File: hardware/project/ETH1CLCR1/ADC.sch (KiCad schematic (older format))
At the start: 53 parts, among them Q1601 BC847, Q1602 BC847, Q1603 BC847, Q1604 BC847, U1601 ADS8363, U1602 INA159, U1603 INA159, U1604 ADG419BR, U1605 ADG419BR, U1606 OPA602, U1607 OPA602, U1608 PGA103, U1609 PGA103

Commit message: Footprint asigment (not finished).
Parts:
- renumbered C1614 to C1501, C1602 to C1502, C1615 to C1503, C1604 to C1504, C1617 to C1505, C1619 to C1506, C1618 to C1507, C1620 to C1508, C1601 to C1509, C1603 to C1510, C1605 to C1511, C1607 to C1512, C1606 to C1513, C1608 to C1514, C1609 to C1515, C1610 to C1516, C1611 to C1517, C1612 to C1518, C1613 to C1519, C1616 to C1520, Q1601 to Q1501, Q1603 to Q1502, Q1602 to Q1503, Q1604 to Q1504, R1601 to R1501, R1615 to R1502, R1607 to R1503, R1609 to R1504, R1611 to R1505, R1603 to R1506, R1612 to R1507, R1604 to R1508, R1605 to R1509, R1606 to R1510, R1602 to R1511, R1616 to R1512, R1608 to R1513, R1610 to R1514, R1613 to R1515, R1614 to R1516, R1617 to R1517, R1619 to R1518, R1618 to R1519, R1620 to R1520, U1602 to U1501, U1604 to U1502, U1608 to U1503, U1606 to U1504, U1601 to U1505, U1603 to U1506, U1605 to U1507, U1609 to U1508, U1607 to U1509
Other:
- moved on the sheet: C1501, C1502, C1503, C1504, R1501, R1502, R1503, R1504, R1505, R1506, R1507, R1508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

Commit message: Redesinged ADC schematic.
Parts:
- removed C1511, C1513, C1515, C1517, C1519: 100n, Capacitor_SMD:C_0603_1608Metric_Pad1.05x0.95mm_HandSolder, symbol Device:C
- removed C1514, C1516, C1518, C1520: 10u, Capacitor_SMD:C_0805_2012Metric_Pad1.15x1.40mm_HandSolder, symbol Device:C
- removed U1501, U1506: INA159, Package_SO:MSOP-8_3x3mm_P0.65mm, symbol ETH1CLCR1:INA159
- removed U1505: ADS8363, Package_DFN_QFN:QFN-32-1EP_5x5mm_P0.5mm_EP3.6x3.6mm_ThermalVias, symbol ETH1CLCR1:ADS8363
- added C1501, C1504, C1505, C1507: 1u, Capacitor_SMD:C_0603_1608Metric_Pad1.05x0.95mm_HandSolder, symbol Device:C
- added C1502, C1506, C1508: 100n, Capacitor_SMD:C_0603_1608Metric_Pad1.05x0.95mm_HandSolder, symbol Device:C
- added R1501, R1502: 100, Resistor_SMD:R_0603_1608Metric_Pad1.05x0.95mm_HandSolder, symbol Device:R
- added R1503, R1504, R1512, R1514: 10k, Resistor_SMD:R_0603_1608Metric_Pad1.05x0.95mm_HandSolder, symbol Device:R
- added R1507, R1515, R1516: 52k3, Resistor_SMD:R_0603_1608Metric_Pad1.05x0.95mm_HandSolder, symbol Device:R
- added R1513: 12k, Resistor_SMD:R_0603_1608Metric_Pad1.05x0.95mm_HandSolder, symbol Device:R
- added U1503: AD8606-2-MSOP, symbol ETH1CLCR1:AD8606-2-MSOP
- added U1504: AD7380, symbol ETH1CLCR1:AD7380
- added U1505: AD8605, symbol ETH1CLCR1:AD8605
- C1503: value 1n -> 100n
- C1510: value 10u -> 100n; footprint Capacitor_SMD:C_0805_2012Metric_Pad1.15x1.40mm_HandSolder -> Capacitor_SMD:C_0603_1608Metric_Pad1.05x0.95mm_HandSolder
- C1512: value 10u -> 1n; footprint Capacitor_SMD:C_0805_2012Metric_Pad1.15x1.40mm_HandSolder -> Capacitor_SMD:C_0603_1608Metric_Pad1.05x0.95mm_HandSolder
- R1506: value 0 -> 100
- R1508: value 0 -> 52k3
- R1509, R1510: value 0 -> 12k
- R1511: value 100 -> 12k
- renumbered C1501 to C1511, C1505 to C1513, C1507 to C1514, C1502 to C1515, C1504 to C1516, C1506 to C1517, C1508 to C1518, Q1503 to Q1502, Q1502 to Q1503, R1501 to R1505, R1503 to R1517, R1513 to R1518, R1504 to R1519, R1514 to R1520, R1505 to R1521, R1507 to R1522, R1515 to R1523, R1516 to R1524, R1517 to R1525, R1519 to R1526, R1502 to R1527, R1512 to R1528, R1518 to R1529, R1520 to R1530, U1507 to U1501, U1504 to U1506, U1509 to U1507, U1503 to U1508, U1508 to U1509
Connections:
- net labels added: ADC_REF, ADC_SCLK, ADC_~ALARM, REFIO
- net labels removed: ADC_BUSY, ADC_CLOCK, ADC_CONVST, ADC_RD
- wire segments 246 -> 207
- no-connect marks 7 -> 4
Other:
- moved on the sheet: C1511, C1515, C1516, R1505, R1517, R1518, R1519, R1520, R1521, R1522, R1523, R1524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

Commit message: Redesigned the power supply, added humidy+temp. sensor.
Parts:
- removed R1503, R1504: 10k, Resistor_SMD:R_0603_1608Metric_Pad1.05x0.95mm_HandSolder, symbol Device:R
- added C1103, C1105: 1u, Capacitor_SMD:C_0603_1608Metric_Pad1.05x0.95mm_HandSolder, symbol Device:C
- added C1108, C1109: 3300p, Capacitor_SMD:C_0603_1608Metric_Pad1.05x0.95mm_HandSolder, symbol Device:C
- added C1110, C1111, C1112, C1113: 100n, Capacitor_SMD:C_0603_1608Metric_Pad1.05x0.95mm_HandSolder, symbol Device:C
- added R1103, R1104: 1k, Resistor_SMD:R_0603_1608Metric_Pad1.05x0.95mm_HandSolder, symbol Device:R
- added R1105, R1106, R1107, R1108: 100, Resistor_SMD:R_0603_1608Metric_Pad1.05x0.95mm_HandSolder, symbol Device:R
- added R1109, R1110, R1111, R1112: 50, Resistor_SMD:R_0603_1608Metric_Pad1.05x0.95mm_HandSolder, symbol Device:R
- added U1105: AD8605, Package_TO_SOT_SMD:SOT-23-5_HandSoldering, symbol ETH1CLCR1:AD8605
- added U1107, U1108: LT6350, Package_SO:MSOP-8_3x3mm_P0.65mm, symbol ETH1CLCR1:LT6350
- U1103: renamed from U1503; footprint (none) -> Package_SO:MSOP-8_3x3mm_P0.65mm
- U1104: renamed from U1504; footprint (none) -> Package_CSP:LFCSP-16-1EP_3x3mm_P0.5mm_EP1.6x1.6mm
- U1106: renamed from U1505; footprint (none) -> Package_TO_SOT_SMD:SOT-23-5_HandSoldering
- renumbered C1501 to C1101, C1503 to C1102, C1507 to C1104, C1504 to C1106, C1505 to C1107, C1502 to C1114, C1511 to C1115, C1512 to C1116, C1506 to C1117, C1508 to C1118, C1509 to C1119, C1510 to C1120, C1513 to C1121, C1514 to C1122, C1515 to C1123, C1516 to C1124, C1517 to C1125, C1518 to C1126, Q1501 to Q1101, Q1502 to Q1102, Q1503 to Q1103, Q1504 to Q1104, R1501 to R1101, R1502 to R1102, R1507 to R1113, R1505 to R1114, R1508 to R1115, R1506 to R1116, R1509 to R1117, R1510 to R1118, R1511 to R1119, R1512 to R1120, R1513 to R1121, R1514 to R1122, R1515 to R1123, R1516 to R1124, R1517 to R1125, R1518 to R1126, R1519 to R1127, R1520 to R1128, R1521 to R1129, R1522 to R1130, R1523 to R1131, R1524 to R1132, R1525 to R1133, R1526 to R1134, R1527 to R1135, R1528 to R1136, R1529 to R1137, R1530 to R1138, U1501 to U1101, U1502 to U1102, U1506 to U1109, U1507 to U1110, U1508 to U1111, U1509 to U1112
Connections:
- net +3.3VF: now also C1103.1, C1105.1
- net +5VF: now also C1110.1, C1111.1, C1112.1, C1113.1, U1105.5 (V+), U1107.3 (V+), U1107.7 (~SHDN), U1108.3 (V+), U1108.7 (~SHDN)
- net ADC_REF: now also U1105.1, U1105.4 (-); no longer U1106.1, U1106.4 (-)
- net AGNDF: now also C1103.2, C1105.2, C1110.2, C1111.2, C1112.2, C1113.2, R1104.2, U1105.2 (V-), U1107.6 (V-), U1108.6 (V-)
- net REFIO: now also R1103.2, U1105.3 (+); no longer U1106.3 (+)
- net at C1115.1, R1114.2: now also U1107.8 (+IN1); no longer U1104.8 (AINA+)
- net at C1116.1, R1116.2: now also U1108.8 (+IN1); no longer U1104.6 (AINB+)
- net at U1104.7 (AINA-): now also R1106.2; no longer U1104.5 (AINB-)
- new net: R1103.1, R1104.1, U1106.3 (+)
- new net: R1109.1, U1107.1 (-IN1), U1107.4 (OUT1)
- new net: R1110.1, U1107.5 (OUT2)
- new net: R1111.1, U1108.1 (-IN1), U1108.4 (OUT1)
- new net: R1112.1, U1108.5 (OUT2)
- new net: C1108.1, R1105.1, R1109.2
- new net: C1108.2, R1106.1, R1110.2
- new net: R1105.2, U1104.8 (AINA+)
- new net: C1109.1, R1107.1, R1111.2
- new net: C1109.2, R1108.1, R1112.2
- new net: R1107.2, U1104.6 (AINB+)
- new net: R1108.2, U1104.5 (AINB-)
- new net VCM: U1106.1, U1106.4 (-), U1107.2 (+IN2), U1108.2 (+IN2)
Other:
- moved on the sheet: C1101, C1102, C1104, C1106, C1107, C1114, C1117, C1118, C1119, C1120, R1101, R1102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

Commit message: PCB layout
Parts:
- added R1139, R1140: 499, Resistor_SMD:R_0603_1608Metric_Pad1.05x0.95mm_HandSolder, symbol Device:R
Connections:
- net VCM: now also R1139.2, R1140.2; no longer U1107.2 (+IN2), U1108.2 (+IN2)
- new net: R1139.1, U1107.2 (+IN2)
- new net: R1140.1, U1108.2 (+IN2)
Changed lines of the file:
@@
 	1    0    0    -1
 $EndComp
-Text Label 7600 3150 1    50   ~ 0
+Text Label 7600 3450 1    50   ~ 0
 VCM
 Wire Wire Line
-	7600 3150 7600 2950
-Text Label 7600 6050 1    50   ~ 0
-VCM
-Wire Wire Line
-	7600 6050 7600 5850
-Wire Wire Line
-	7900 5850 7900 6150
-Wire Wire Line
-	7900 6150 6450 6150
-Wire Wire Line
-	6450 6150 6450 5050
+	7600 3450 7600 3250
 Wire Wire Line
 	6450 5050 6550 5050
 Wire Wire Line
-	7900 2950 7900 3250
-Wire Wire Line
-	7900 3250 6450 3250
-Wire Wire Line
-	6450 3250 6450 2150
+	7900 2950 7900 3550
+Wire Wire Line
+	7900 3550 6450 3550
+Wire Wire Line
+	6450 3550 6450 2150
 Wire Wire Line
 	6550 2150 6450 2150
@@
 	1    0    0    -1
 $EndComp
+$Comp
+L Device:R R1139
+U 1 1 5E246E09
+P 7600 3100
+F 0 "R1139" H 7650 3150 50  0000 L CNN
+F 1 "499" H 7670 3055 50  0000 L CNN
+F 2 "Resistor_SMD:R_0603_1608Metric_Pad1.05x0.95mm_HandSolder" V 7530 3100 50  0001 C CNN
+F 3 "~" H 7600 3100 50  0001 C CNN
+	1    7600 3100
+	1    0    0    -1
+$EndComp
+Wire Wire Line
+	7900 5850 7900 6450
+Wire Wire Line
+	7900 6450 6450 6450
+Wire Wire Line
+	6450 5050 6450 6450
+Text Label 7600 6350 1    50   ~ 0
+VCM
+Wire Wire Line
+	7600 6350 7600 6150
+$Comp
+L Device:R R1140
+U 1 1 5E310DDA
+P 7600 6000
+F 0 "R1140" H 7650 6050 50  0000 L CNN
+F 1 "499" H 7670 5955 50  0000 L CNN
+F 2 "Resistor_SMD:R_0603_1608Metric_Pad1.05x0.95mm_HandSolder" V 7530 6000 50  0001 C CNN
+F 3 "~" H 7600 6000 50  0001 C CNN
+	1    7600 6000
+	1    0    0    -1
+$EndComp

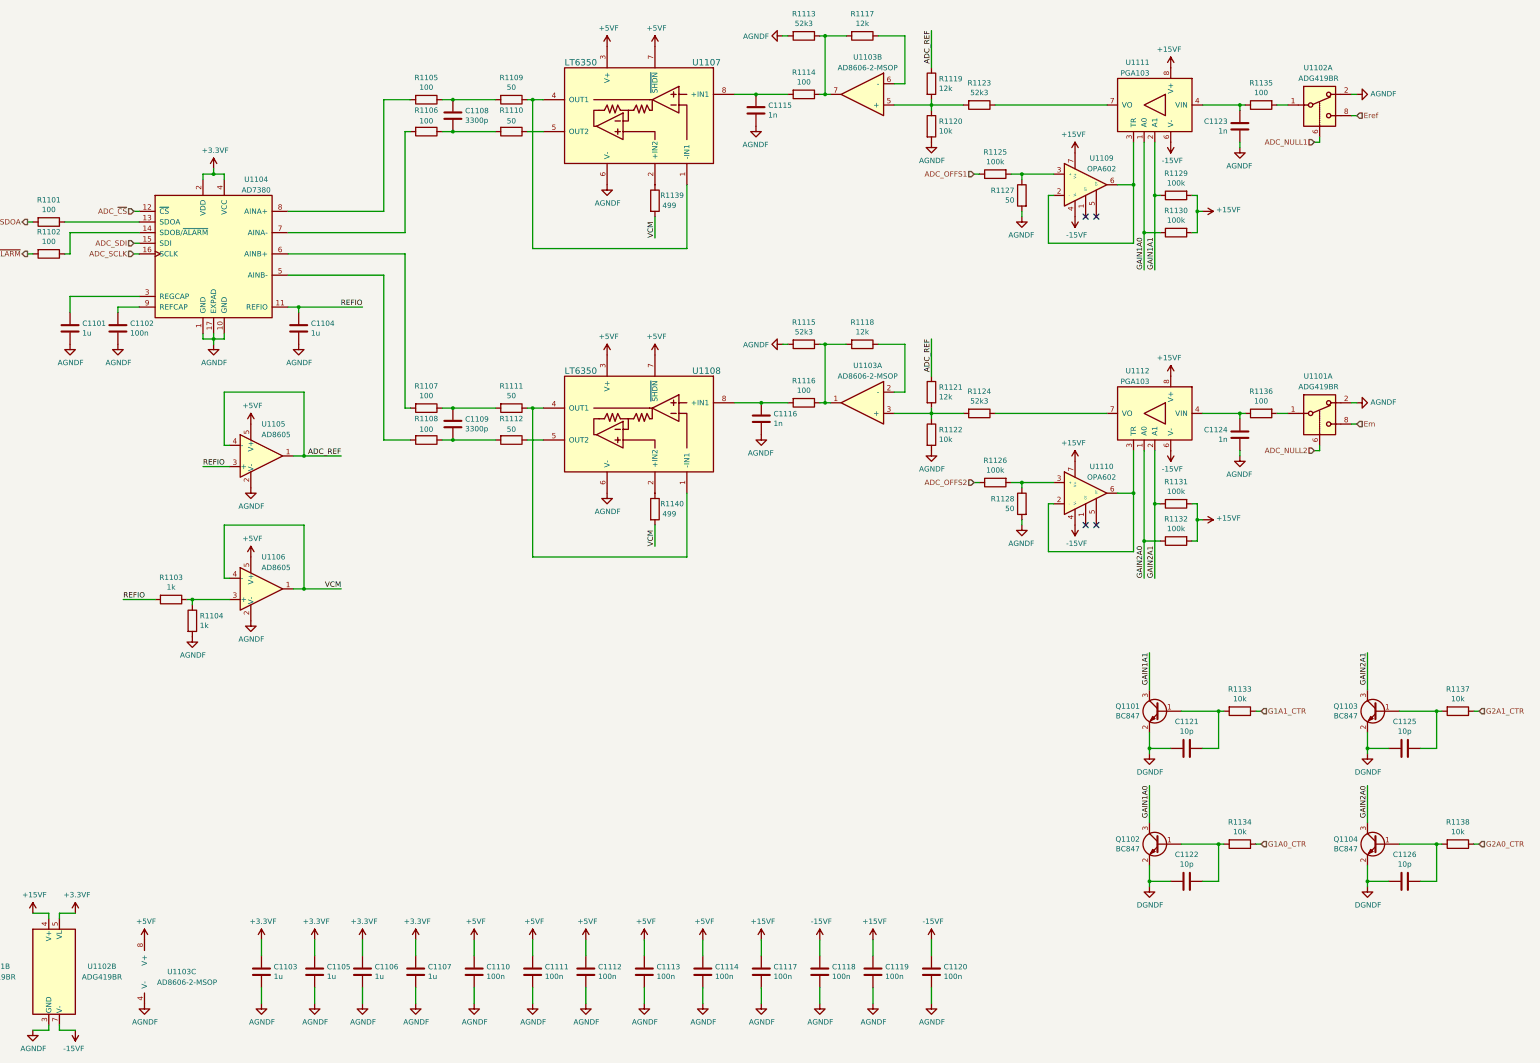
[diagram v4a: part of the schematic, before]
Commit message: Fixed mistake in ADC schematic.
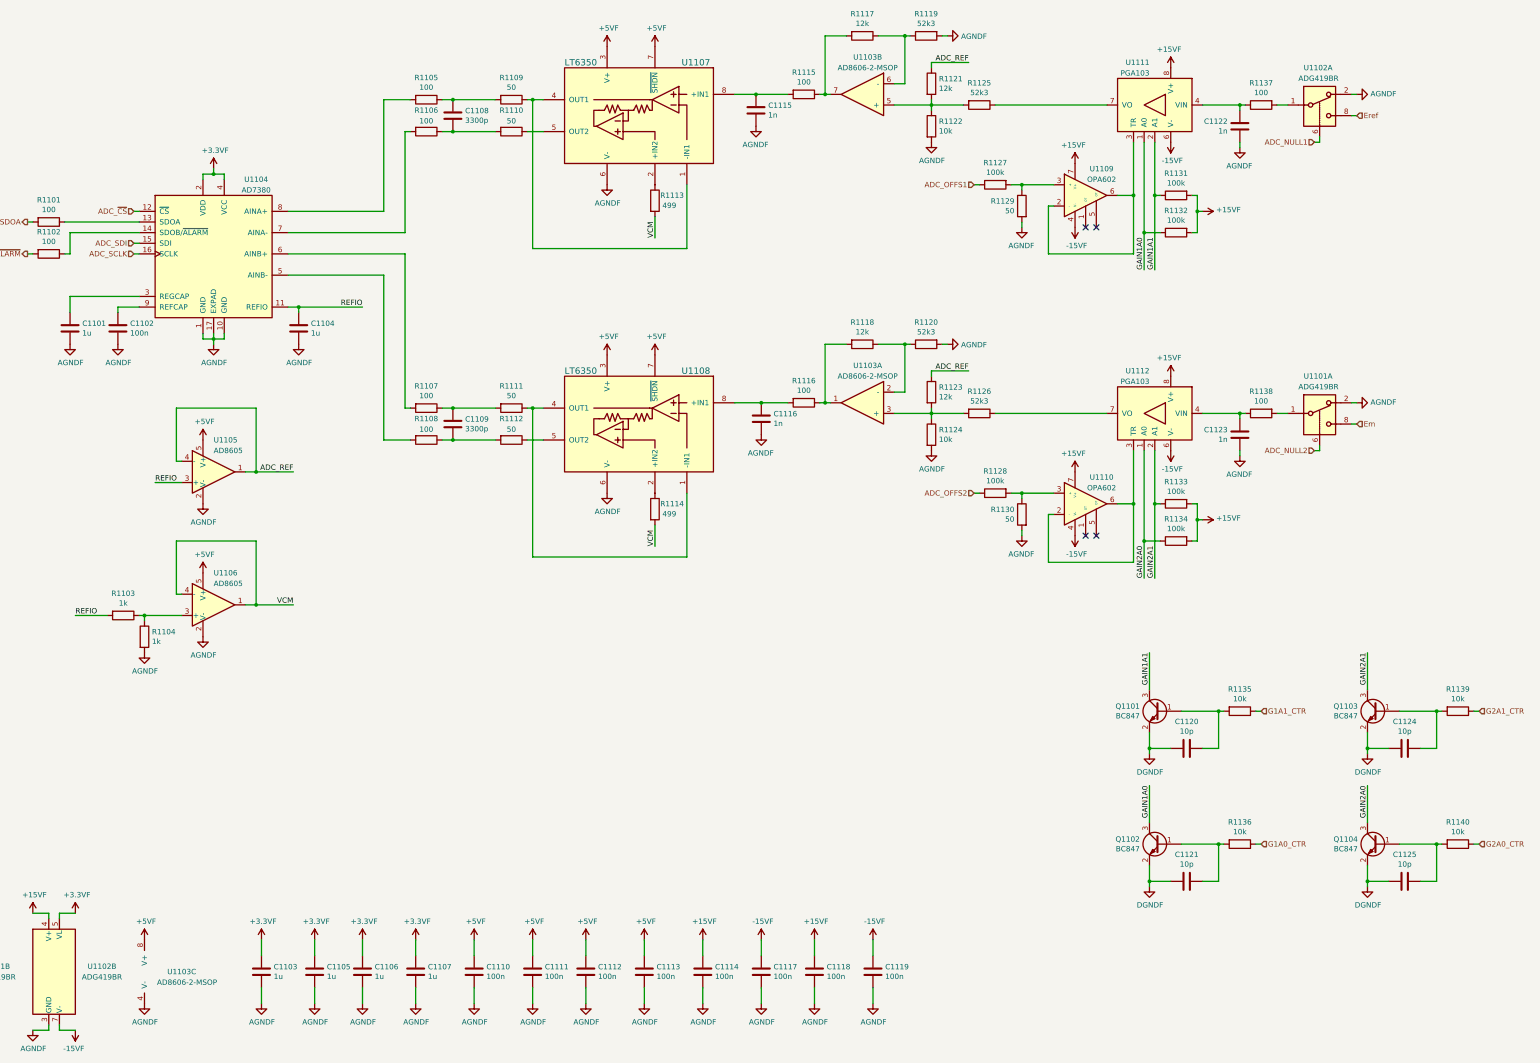
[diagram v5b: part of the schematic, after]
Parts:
- removed C1114: 100n, Capacitor_SMD:C_0603_1608Metric_Pad1.05x0.95mm_HandSolder, symbol Device:C
- renumbered C1117 to C1114, C1118 to C1117, C1119 to C1118, C1120 to C1119, C1121 to C1120, C1122 to C1121, C1123 to C1122, C1124 to C1123, C1125 to C1124, C1126 to C1125, R1139 to R1113, R1140 to R1114, R1114 to R1115, R1113 to R1119, R1115 to R1120, R1119 to R1121, R1120 to R1122, R1121 to R1123, R1122 to R1124, R1123 to R1125, R1124 to R1126, R1125 to R1127, R1126 to R1128, R1127 to R1129, R1128 to R1130, R1129 to R1131, R1130 to R1132, R1131 to R1133, R1132 to R1134, R1133 to R1135, R1134 to R1136, R1135 to R1137, R1136 to R1138, R1137 to R1139, R1138 to R1140
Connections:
- net at R1115.1, R1117.2, U1103.7: no longer R1119.1
- net at R1117.1, U1103.6 (-): now also R1119.1
- net at R1116.1, R1118.2, U1103.1: no longer R1120.1
- net at R1118.1, U1103.2 (-): now also R1120.1
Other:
- moved on the sheet: C1114, C1117, C1118, C1119, R1103, R1104, R1119, R1120, R1127, R1128, R1129, R1130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

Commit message: Changes in schematics.
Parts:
- removed U1105, U1106: AD8605, Package_TO_SOT_SMD:SOT-23-5_HandSoldering, symbol ETH1CLCR1:AD8605
- added C1101, C1106, C1114: 100n, Capacitor_SMD:C_0603_1608Metric_Pad1.05x0.95mm_HandSolder, symbol Device:C
- added C1102: 10u, Capacitor_SMD:C_0805_2012Metric_Pad1.15x1.40mm_HandSolder, symbol Device:C
- added C1104: 1u, Capacitor_SMD:C_0603_1608Metric_Pad1.05x0.95mm_HandSolder, symbol Device:C
- added U1103: REF192, Package_SO:SSOP-8_3.9x5.05mm_P1.27mm, symbol Reference_Voltage:REF192
- added U1105: AD8606-2-MSOP, Package_SO:MSOP-8_3x3mm_P0.65mm, symbol ETH1CLCR1:AD8606-2-MSOP
- added U1107: AD8605, Package_TO_SOT_SMD:SOT-23-5_HandSoldering, symbol ETH1CLCR1:AD8605
- R1103, R1104: value 1k -> 10k
- renumbered C1101 to C1103, C1102 to C1105, C1104 to C1107, C1103 to C1108, C1105 to C1109, C1106 to C1110, C1108 to C1111, C1109 to C1112, C1107 to C1113, C1110 to C1115, C1111 to C1116, C1112 to C1117, C1115 to C1118, C1116 to C1119, C1113 to C1120, C1114 to C1121, C1117 to C1122, C1118 to C1123, C1119 to C1124, C1120 to C1125, C1121 to C1126, C1122 to C1127, C1123 to C1128, C1124 to C1129, C1125 to C1130, U1103 to U1104, U1104 to U1106, U1107 to U1108, U1108 to U1109, U1109 to U1110, U1110 to U1111, U1111 to U1112, U1112 to U1113
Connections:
- net +5VF: now also C1101.1, C1102.1, C1114.1, U1103.2 (Vin), U1103.3 (~Sleep~), U1105.8 (V+), U1107.5 (V+)
- net ADC_REF: now also U1105.1, U1105.2 (-)
- net AGNDF: now also C1101.2, C1102.2, C1104.2, C1106.2, C1114.2, U1103.4 (GND), U1105.4 (V-), U1107.2 (V-)
- net REFIO: now also U1105.3 (+), U1107.1, U1107.4 (-)
- net VCM: now also U1105.6 (-), U1105.7
- net at R1103.1, R1104.1: now also U1105.5 (+)
- new net: C1104.1, C1106.1, U1103.6 (Vout), U1107.3 (+)
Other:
- note added: "Place reistors close to the ADC chip."
- moved on the sheet: C1103, C1108, C1109, C1110, C1113, C1115, C1116, C1117, C1120, C1121, C1122, C1123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

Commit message: Checked the schematics. Created BOM.
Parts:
- removed Q1101, Q1102, Q1103, Q1104: BC847, Package_TO_SOT_SMD:SOT-23, symbol Transistor_BJT:BC847
- added Q1101, Q1102, Q1103, Q1104: BC847W, Package_TO_SOT_SMD:SOT-323_SC-70, symbol Transistor_BJT:BC847W
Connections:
- net DGNDF: now also Q1101.2 (E), Q1102.2 (E), Q1103.2 (E), Q1104.2 (E)
- net GAIN1A0: now also Q1102.3 (C)
- net GAIN1A1: now also Q1101.3 (C)
- net GAIN2A0: now also Q1104.3 (C)
- net GAIN2A1: now also Q1103.3 (C)
- net at C1126.1, R1136.2: now also Q1102.1 (B)
- net at C1125.1, R1135.2: now also Q1101.1 (B)
- net at C1130.1, R1140.2: now also Q1104.1 (B)
- net at C1129.1, R1139.2: now also Q1103.1 (B)
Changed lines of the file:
@@
 	0    1    1    0
-$EndComp
-$Comp
-L Transistor_BJT:BC847 Q?
-U 1 1 5E39CEF2
-P 12350 9150
-AR Path="/5DF36410/5E39CEF2" Ref="Q?"  Part="1"
-AR Path="/5DED09C5/5E39CEF2" Ref="Q?"  Part="1"
-AR Path="/5E22FF57/5E39CEF2" Ref="Q?"  Part="1"
-AR Path="/5E402F62/5E39CEF2" Ref="Q1102"  Part="1"
-F 0 "Q1102" H 12541 9196 50  0000 L CNN
-F 1 "BC847" H 12541 9105 50  0000 L CNN
-F 2 "Package_TO_SOT_SMD:SOT-23" H 12550 9075 50  0001 L CIN
-F 3 "http://www.infineon.com/dgdl/Infineon-BC847SERIES_BC848SERIES_BC849SERIES_BC850SERIES-DS-v01_01-en.pdf?fileId=db3a304314dca389011541d4630a1657" H 12350 9150 50  0001 L CNN
-	1    12350 9150
-	-1   0    0    -1
 $EndComp
 Text Label 12250 8600 3    50   ~ 0
@@
 	0    1    1    0
 $EndComp
-$Comp
-L Transistor_BJT:BC847 Q?
-U 1 1 5E39CF3C
-P 14400 9150
-AR Path="/5DF36410/5E39CF3C" Ref="Q?"  Part="1"
-AR Path="/5DED09C5/5E39CF3C" Ref="Q?"  Part="1"
-AR Path="/5E22FF57/5E39CF3C" Ref="Q?"  Part="1"
-AR Path="/5E402F62/5E39CF3C" Ref="Q1104"  Part="1"
-F 0 "Q1104" H 14591 9196 50  0000 L CNN
-F 1 "BC847" H 14591 9105 50  0000 L CNN
-F 2 "Package_TO_SOT_SMD:SOT-23" H 14600 9075 50  0001 L CIN
-F 3 "http://www.infineon.com/dgdl/Infineon-BC847SERIES_BC848SERIES_BC849SERIES_BC850SERIES-DS-v01_01-en.pdf?fileId=db3a304314dca389011541d4630a1657" H 14400 9150 50  0001 L CNN
-	1    14400 9150
-	-1   0    0    -1
-$EndComp
 Text Label 14300 8600 3    50   ~ 0
 GAIN2A0
@@
 	0    1    1    0
 $EndComp
-$Comp
-L Transistor_BJT:BC847 Q?
-U 1 1 5E39CF61
-P 14400 7900
-AR Path="/5DF36410/5E39CF61" Ref="Q?"  Part="1"
-AR Path="/5DED09C5/5E39CF61" Ref="Q?"  Part="1"
-AR Path="/5E22FF57/5E39CF61" Ref="Q?"  Part="1"
-AR Path="/5E402F62/5E39CF61" Ref="Q1103"  Part="1"
-F 0 "Q1103" H 14591 7946 50  0000 L CNN
-F 1 "BC847" H 14591 7855 50  0000 L CNN
-F 2 "Package_TO_SOT_SMD:SOT-23" H 14600 7825 50  0001 L CIN
-F 3 "http://www.infineon.com/dgdl/Infineon-BC847SERIES_BC848SERIES_BC849SERIES_BC850SERIES-DS-v01_01-en.pdf?fileId=db3a304314dca389011541d4630a1657" H 14400 7900 50  0001 L CNN
-	1    14400 7900
-	-1   0    0    -1
-$EndComp
 Text Label 14300 7350 3    50   ~ 0
 GAIN2A1
@@
 Connection ~ 800  1700
 $Comp
-L Transistor_BJT:BC847 Q?
-U 1 1 5E39CF17
+L Transistor_BJT:BC847W Q1101
+U 1 1 5E2D720E
 P 12350 7900
-AR Path="/5DF36410/5E39CF17" Ref="Q?"  Part="1"
-AR Path="/5DED09C5/5E39CF17" Ref="Q?"  Part="1"
-AR Path="/5E22FF57/5E39CF17" Ref="Q?"  Part="1"
-AR Path="/5E402F62/5E39CF17" Ref="Q1101"  Part="1"
 F 0 "Q1101" H 12541 7946 50  0000 L CNN
-F 1 "BC847" H 12541 7855 50  0000 L CNN
-F 2 "Package_TO_SOT_SMD:SOT-23" H 12550 7825 50  0001 L CIN
+F 1 "BC847W" H 12541 7855 50  0000 L CNN
+F 2 "Package_TO_SOT_SMD:SOT-323_SC-70" H 12550 7825 50  0001 L CIN
 F 3 "http://www.infineon.com/dgdl/Infineon-BC847SERIES_BC848SERIES_BC849SERIES_BC850SERIES-DS-v01_01-en.pdf?fileId=db3a304314dca389011541d4630a1657" H 12350 7900 50  0001 L CNN
 	1    12350 7900
 	-1   0    0    -1
 $EndComp
+$Comp
+L Transistor_BJT:BC847W Q1103
+U 1 1 5E2DC2B2
+P 14400 7900
+F 0 "Q1103" H 14591 7946 50  0000 L CNN
+F 1 "BC847W" H 14591 7855 50  0000 L CNN
+F 2 "Package_TO_SOT_SMD:SOT-323_SC-70" H 14600 7825 50  0001 L CIN
+F 3 "http://www.infineon.com/dgdl/Infineon-BC847SERIES_BC848SERIES_BC849SERIES_BC850SERIES-DS-v01_01-en.pdf?fileId=db3a304314dca389011541d4630a1657" H 14400 7900 50  0001 L CNN
+	1    14400 7900
+	-1   0    0    -1
+$EndComp
+$Comp
+L Transistor_BJT:BC847W Q1102
+U 1 1 5E2DC789
+P 12350 9150
+F 0 "Q1102" H 12541 9196 50  0000 L CNN
+F 1 "BC847W" H 12541 9105 50  0000 L CNN
+F 2 "Package_TO_SOT_SMD:SOT-323_SC-70" H 12550 9075 50  0001 L CIN
+F 3 "http://www.infineon.com/dgdl/Infineon-BC847SERIES_BC848SERIES_BC849SERIES_BC850SERIES-DS-v01_01-en.pdf?fileId=db3a304314dca389011541d4630a1657" H 12350 9150 50  0001 L CNN
+	1    12350 9150
+	-1   0    0    -1
+$EndComp
+$Comp
+L Transistor_BJT:BC847W Q1104
+U 1 1 5E2DD893
+P 14400 9150
+F 0 "Q1104" H 14591 9196 50  0000 L CNN
+F 1 "BC847W" H 14591 9105 50  0000 L CNN
+F 2 "Package_TO_SOT_SMD:SOT-323_SC-70" H 14600 9075 50  0001 L CIN
+F 3 "http://www.infineon.com/dgdl/Infineon-BC847SERIES_BC848SERIES_BC849SERIES_BC850SERIES-DS-v01_01-en.pdf?fileId=db3a304314dca389011541d4630a1657" H 14400 9150 50  0001 L CNN
+	1    14400 9150
+	-1   0    0    -1
+$EndComp
